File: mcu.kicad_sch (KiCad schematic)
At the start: 27 parts, among them J1 RP_DEBUG, SW1 BOOTSEL, SW2 RESET, U1 W25Q16JVSNIQ, U2 RP2040, Y1 12MHz

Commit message: WIP: display
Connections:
- net CAN_~{CS}: now also U2.7 (GPIO5); no longer U2.3 (GPIO1)
- net CAN_~{INT}: now also U2.3 (GPIO1); no longer U2.7 (GPIO5)
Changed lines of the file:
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@@
     (effects (font (size 1 1)) (justify left))
   )
-  (hierarchical_label "CAN_~{INT}" (shape input) (at 215.9 81.28 0)
+  (hierarchical_label "CAN_~{INT}" (shape input) (at 215.9 71.12 0)
     (effects (font (size 1 1)) (justify left))
   )
-  (hierarchical_label "CAN_~{CS}" (shape output) (at 215.9 71.12 0)
+  (hierarchical_label "CAN_~{CS}" (shape output) (at 215.9 81.28 0)
     (effects (font (size 1 1)) (justify left))
   )

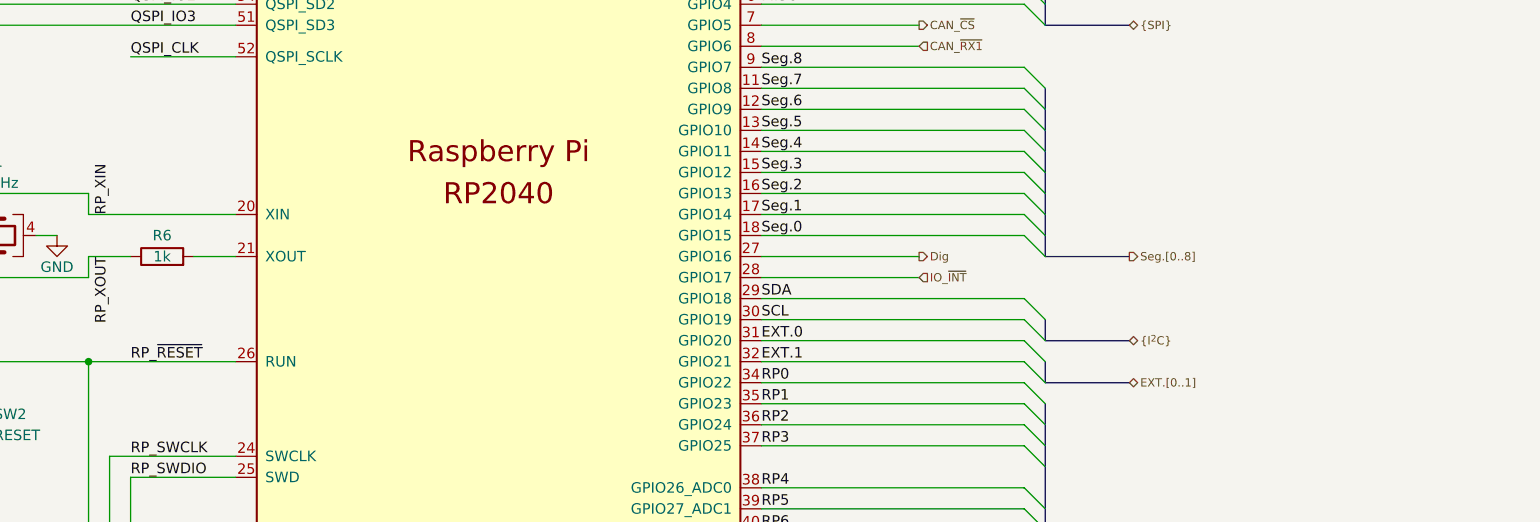
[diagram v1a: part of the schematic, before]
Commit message: rev1.1: Add I2C pullups
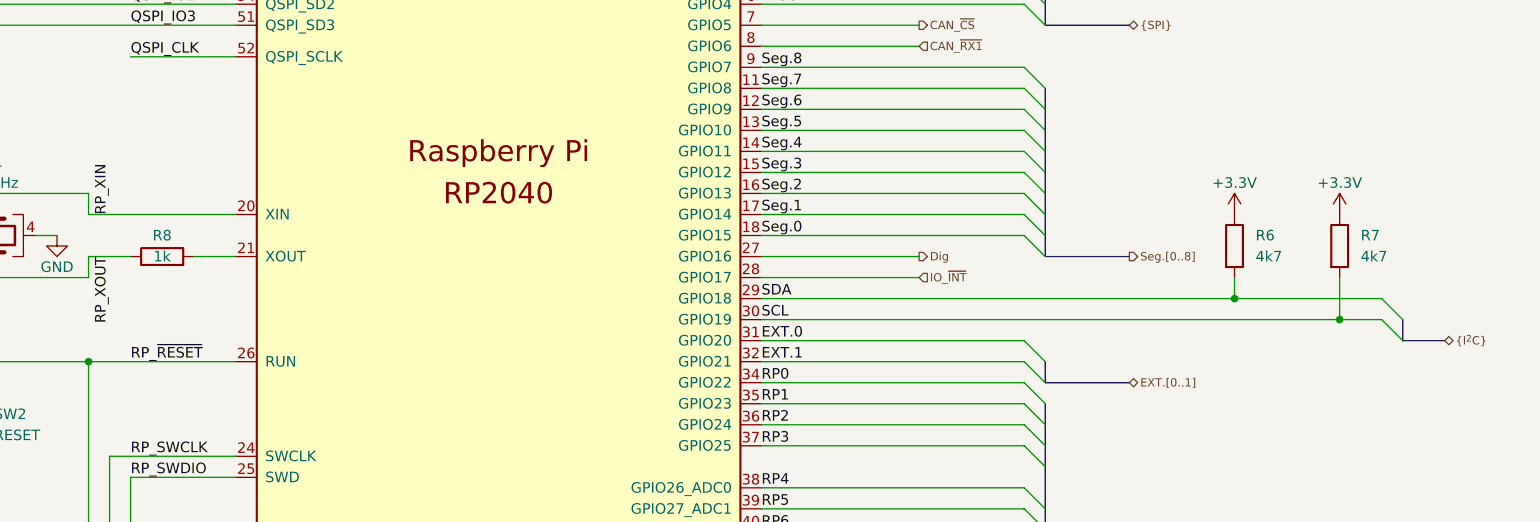
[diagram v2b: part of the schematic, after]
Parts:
- added R6, R7: 4k7, Resistor_SMD:R_0603_1608Metric, symbol Device:R
- renumbered R6 to R8
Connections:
- net +3V3: now also R6.1, R7.1
- net SCL: now also R7.2
- net SDA: now also R6.2
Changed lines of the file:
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@@
   (title_block
     (title "[canbrd] CAN/RS485 IO board")
-    (date "2022-02-24")
-    (rev "1.0")
+    (date "2022-03-18")
+    (rev "1.1")
   )
   (junction (at 173.99 48.26) (diameter 0) (color 0 0 0 0)
@@
   (junction (at 166.37 48.26) (diameter 0) (color 0 0 0 0)
   )
+  (junction (at 254 114.3) (diameter 0) (color 0 0 0 0)
+  )
   (junction (at 177.8 25.4) (diameter 0) (color 0 0 0 0)
   )
@@
   )
   (junction (at 127 38.1) (diameter 0) (color 0 0 0 0)
+  )
+  (junction (at 266.7 116.84) (diameter 0) (color 0 0 0 0)
   )
   (junction (at 85.09 111.76) (diameter 0) (color 0 0 0 0)
@@
     (stroke (width 0) (type default) (color 0 0 0 0))
   )
-  (bus_entry (at 231.14 116.84) (size -2.54 -2.54)
+  (bus_entry (at 274.32 116.84) (size -2.54 -2.54)
     (stroke (width 0) (type default) (color 0 0 0 0))
   )
@@
     (stroke (width 0) (type default) (color 0 0 0 0))
   )
-  (bus_entry (at 231.14 119.38) (size -2.54 -2.54)
+  (bus_entry (at 274.32 119.38) (size -2.54 -2.54)
     (stroke (width 0) (type default) (color 0 0 0 0))
   )
@@
     (stroke (width 0) (type default) (color 0 0 0 0))
   )
-  (wire (pts (xy 196.85 116.84) (xy 228.6 116.84))
+  (wire (pts (xy 196.85 116.84) (xy 266.7 116.84))
     (stroke (width 0) (type default) (color 0 0 0 0))
   )
@@
     (stroke (width 0) (type default) (color 0 0 0 0))
   )
+  (wire (pts (xy 266.7 111.76) (xy 266.7 116.84))
+    (stroke (width 0) (type default) (color 0 0 0 0))
+  )
   (wire (pts (xy 152.4 25.4) (xy 165.1 25.4))
     (stroke (width 0) (type default) (color 0 0 0 0))
@@
     (stroke (width 0) (type default) (color 0 0 0 0))
   )
+  (wire (pts (xy 254 114.3) (xy 271.78 114.3))
+    (stroke (width 0) (type default) (color 0 0 0 0))
+  )
   (wire (pts (xy 115.57 109.22) (xy 120.65 109.22))
     (stroke (width 0) (type default) (color 0 0 0 0))
@@
     (stroke (width 0) (type default) (color 0 0 0 0))
   )
-  (bus (pts (xy 241.3 119.38) (xy 231.14 119.38))
+  (bus (pts (xy 279.4 119.38) (xy 274.32 119.38))
     (stroke (width 0) (type default) (color 0 0 0 0))
   )
@@
     (stroke (width 0) (type default) (color 0 0 0 0))
   )
+  (wire (pts (xy 266.7 116.84) (xy 271.78 116.84))
+    (stroke (width 0) (type default) (color 0 0 0 0))
+  )
   (wire (pts (xy 177.8 35.56) (xy 177.8 38.1))
     (stroke (width 0) (type default) (color 0 0 0 0))
@@
     (stroke (width 0) (type default) (color 0 0 0 0))
   )
+  (wire (pts (xy 254 111.76) (xy 254 114.3))
+    (stroke (width 0) (type default) (color 0 0 0 0))
+  )
   (wire (pts (xy 196.85 81.28) (xy 215.9 81.28))
     (stroke (width 0) (type default) (color 0 0 0 0))
   )
-  (wire (pts (xy 196.85 114.3) (xy 228.6 114.3))
+  (wire (pts (xy 196.85 114.3) (xy 254 114.3))
     (stroke (width 0) (type default) (color 0 0 0 0))
   )
@@
     (stroke (width 0) (type default) (color 0 0 0 0))
   )
-  (bus (pts (xy 231.14 116.84) (xy 231.14 119.38))
+  (bus (pts (xy 274.32 116.84) (xy 274.32 119.38))
     (stroke (width 0) (type default) (color 0 0 0 0))
   )
@@
     (effects (font (size 1 1)) (justify left))
   )
-  (hierarchical_label "{I^{2}C}" (shape bidirectional) (at 241.3 119.38 0)
+  (hierarchical_label "{I^{2}C}" (shape bidirectional) (at 279.4 119.38 0)
     (effects (font (size 1 1)) (justify left))
   )
   (symbol (lib_id "power:GND") (at 76.2 167.64 0) (unit 1)
     (in_bom yes) (on_board yes)
-    (property "Reference" "#PWR027" (id 0) (at 76.2 173.99 0)
+    (property "Reference" "#PWR029" (id 0) (at 76.2 173.99 0)
       (effects (font (size 1.27 1.27)) hide)
     )
@@
   (symbol (lib_id "Device:R") (at 124.46 109.22 90) (unit 1)
     (in_bom yes) (on_board yes)
-    (property "Reference" "R6" (id 0) (at 124.46 106.68 90))
+    (property "Reference" "R8" (id 0) (at 124.46 106.68 90))
     (property "Value" "1k" (id 1) (at 124.46 109.22 90))
     (property "Footprint" "Resistor_SMD:R_0603_1608Metric" (id 2) (at 124.46 110.998 90)
@@
     (pin "2")
   )
+  (symbol (lib_id "power:+3.3V") (at 254 104.14 0) (unit 1)
+    (in_bom yes) (on_board yes)
+    (property "Reference" "#PWR021" (id 0) (at 254 107.95 0)
+      (effects (font (size 1.27 1.27)) hide)
+    )
+    (property "Value" "+3.3V" (id 1) (at 254 100.33 0))
+    (property "Footprint" "" (id 2) (at 254 104.14 0)
+      (effects (font (size 1.27 1.27)) hide)
+    )
+    (property "Datasheet" "" (id 3) (at 254 104.14 0)
+      (effects (font (size 1.27 1.27)) hide)
+    )
+    (pin "1")
+  )
   (symbol (lib_id "Device:C") (at 165.1 31.75 0) (unit 1)
     (in_bom yes) (on_board yes)
@@
   (symbol (lib_id "power:GND") (at 101.6 134.62 0) (unit 1)
     (in_bom yes) (on_board yes)
-    (property "Reference" "#PWR023" (id 0) (at 101.6 140.97 0)
+    (property "Reference" "#PWR025" (id 0) (at 101.6 140.97 0)
       (effects (font (size 1.27 1.27)) hide)
     )
@@
   (symbol (lib_id "power:GND") (at 111.76 106.68 0) (unit 1)
     (in_bom yes) (on_board yes)
-    (property "Reference" "#PWR021" (id 0) (at 111.76 113.03 0)
+    (property "Reference" "#PWR023" (id 0) (at 111.76 113.03 0)
       (effects (font (size 1.27 1.27)) hide)
     )
@@
     (pin "8")
     (pin "9")
+  )
+  (symbol (lib_id "Device:R") (at 254 107.95 0) (unit 1)
+    (in_bom yes) (on_board yes) (fields_autoplaced)
+    (property "Reference" "R6" (id 0) (at 256.54 106.6799 0)
+      (effects (font (size 1.27 1.27)) (justify left))
+    )
+    (property "Value" "4k7" (id 1) (at 256.54 109.2199 0)
+      (effects (font (size 1.27 1.27)) (justify left))
+    )
+    (property "Footprint" "Resistor_SMD:R_0603_1608Metric" (id 2) (at 252.222 107.95 90)
+      (effects (font (size 1.27 1.27)) hide)
+    )
+    (property "Datasheet" "~" (id 3) (at 254 107.95 0)
+      (effects (font (size 1.27 1.27)) hide)
+    )
+    (pin "1")
+    (pin "2")
   )
   (symbol (lib_id "power:GND") (at 88.9 86.36 0) (unit 1)
@@
   (symbol (lib_id "power:+3.3V") (at 76.2 137.16 0) (unit 1)
     (in_bom yes) (on_board yes)
-    (property "Reference" "#PWR024" (id 0) (at 76.2 140.97 0)
+    (property "Reference" "#PWR026" (id 0) (at 76.2 140.97 0)
       (effects (font (size 1.27 1.27)) hide)
     )
@@
   (symbol (lib_id "power:GND") (at 152.4 152.4 0) (unit 1)
     (in_bom yes) (on_board yes)
-    (property "Reference" "#PWR025" (id 0) (at 152.4 158.75 0)
+    (property "Reference" "#PWR027" (id 0) (at 152.4 158.75 0)
       (effects (font (size 1.27 1.27)) hide)
     )
@@
     (pin "2")
   )
+  (symbol (lib_id "Device:R") (at 266.7 107.95 0) (unit 1)
+    (in_bom yes) (on_board yes) (fields_autoplaced)
+    (property "Reference" "R7" (id 0) (at 269.24 106.6799 0)
+      (effects (font (size 1.27 1.27)) (justify left))
+    )
+    (property "Value" "4k7" (id 1) (at 269.24 109.2199 0)
+      (effects (font (size 1.27 1.27)) (justify left))
+    )
+    (property "Footprint" "Resistor_SMD:R_0603_1608Metric" (id 2) (at 264.922 107.95 90)
+      (effects (font (size 1.27 1.27)) hide)
+    )
+    (property "Datasheet" "~" (id 3) (at 266.7 107.95 0)
+      (effects (font (size 1.27 1.27)) hide)
+    )
+    (pin "1")
+    (pin "2")
+  )
   (symbol (lib_id "Device:R") (at 57.15 82.55 0) (unit 1)
     (in_bom yes) (on_board yes)
@@
   (symbol (lib_id "power:GND") (at 85.09 114.3 0) (unit 1)
     (in_bom yes) (on_board yes)
-    (property "Reference" "#PWR022" (id 0) (at 85.09 120.65 0)
+    (property "Reference" "#PWR024" (id 0) (at 85.09 120.65 0)
       (effects (font (size 1.27 1.27)) hide)
     )
@@
   (symbol (lib_id "power:GND") (at 165.1 152.4 0) (unit 1)
     (in_bom yes) (on_board yes)
-    (property "Reference" "#PWR026" (id 0) (at 165.1 158.75 0)
+    (property "Reference" "#PWR028" (id 0) (at 165.1 158.75 0)
       (effects (font (size 1.27 1.27)) hide)
     )
@@
     (pin "2")
   )
+  (symbol (lib_id "power:+3.3V") (at 266.7 104.14 0) (unit 1)
+    (in_bom yes) (on_board yes)
+    (property "Reference" "#PWR022" (id 0) (at 266.7 107.95 0)
+      (effects (font (size 1.27 1.27)) hide)
+    )
+    (property "Value" "+3.3V" (id 1) (at 266.7 100.33 0))
+    (property "Footprint" "" (id 2) (at 266.7 104.14 0)
+      (effects (font (size 1.27 1.27)) hide)
+    )
+    (property "Datasheet" "" (id 3) (at 266.7 104.14 0)
+      (effects (font (size 1.27 1.27)) hide)
+    )
+    (pin "1")
+  )
 )

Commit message: lots changed
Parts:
- removed R6, R7: 4k7, Resistor_SMD:R_0603_1608Metric, symbol Device:R
- renumbered R8 to R6
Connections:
- net EXT.0 is gone; now on net RP2: U2.31 (GPIO20)
- net EXT.1 is gone; now on net RP3: U2.32 (GPIO21)
- net SCL is gone; now on net RP1: U2.30 (GPIO19)
- net SDA is gone; now on net RP0: U2.29 (GPIO18)
- net RP0: no longer U2.34 (GPIO22)
- net RP1: no longer U2.35 (GPIO23)
- net RP2: no longer U2.36 (GPIO24)
- net RP3: no longer U2.37 (GPIO25)
- net RP4: now also U2.34 (GPIO22); no longer U2.38 (GPIO26_ADC0)
- net RP5: now also U2.35 (GPIO23); no longer U2.39 (GPIO27_ADC1)
- net RP6: now also U2.36 (GPIO24); no longer U2.40 (GPIO28_ADC2)
- net RP7: now also U2.37 (GPIO25); no longer U2.41 (GPIO29_ADC3)
- net IO_~{INT} renamed IO_~{CS}
- new net RP10: U2.40 (GPIO28_ADC2)
- new net RP11: U2.41 (GPIO29_ADC3)
- new net RP8: U2.38 (GPIO26_ADC0)
- new net RP9: U2.39 (GPIO27_ADC1)

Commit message: things changed
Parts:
- added C14, C17: 100n, Capacitor_SMD:C_0603_1608Metric, symbol Device:C
- added R5, R6: 130, Resistor_SMD:R_0603_1608Metric, symbol Device:R
- added R8: DNP, Resistor_SMD:R_0603_1608Metric, symbol Device:R_Small
- renumbered C14 to C15, C15 to C16, R5 to R7, R6 to R9
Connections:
- net GND: now also C14.2, C17.2
- net MOSI: now also R6.2; no longer U2.5 (GPIO3)
- net RP_~{RESET}: now also C17.1
- net SCK: now also R5.2; no longer U2.4 (GPIO2)
- net ~{BOOTSEL}: now also C14.1
- net RP_SWCLK renamed SWCLK
- net RP_SWDIO renamed SWDIO
- net RP_XIN renamed XIN
- net XIN: now also R8.1
- net RP_XOUT renamed XOUT
- net XOUT: now also R8.2
- net USB_XDM renamed xUSB_DM
- net USB_XDP renamed xUSB_DP
- new net xMOSI: R6.1, U2.5 (GPIO3)
- new net xSCK: R5.1, U2.4 (GPIO2)
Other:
- moved on the sheet: C11, C12, J1, R1, SW2

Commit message: isolate and other stuff
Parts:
- added TP1, TP2, TP3: TestPoint, TestPoint:TestPoint_THTPad_D2.0mm_Drill1.0mm, symbol Connector:TestPoint
- C15, C16: value ??? -> 10p
- R5, R6: value 130 -> 100
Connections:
- net RP_~{RESET}: now also TP1.1
- net SWCLK: now also TP2.1
- net SWDIO: now also TP3.1
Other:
- title: [canbrd] CAN/RS485 IO board -> [canbrd] CAN IO board

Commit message: things changed
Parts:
- added R10, R11: 2.2k, Resistor_SMD:R_0603_1608Metric, symbol Device:R
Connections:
- net CAN_~{RX1} is gone; now on net Seg.8: U2.8 (GPIO6)
- net Seg.0: now also U2.17 (GPIO14); no longer U2.18 (GPIO15)
- net Seg.1: now also U2.16 (GPIO13); no longer U2.17 (GPIO14)
- net Seg.2: now also U2.15 (GPIO12); no longer U2.16 (GPIO13)
- net Seg.3: now also U2.14 (GPIO11); no longer U2.15 (GPIO12)
- net Seg.4: now also U2.13 (GPIO10); no longer U2.14 (GPIO11)
- net Seg.5: now also U2.12 (GPIO9); no longer U2.13 (GPIO10)
- net Seg.6: now also U2.11 (GPIO8); no longer U2.12 (GPIO9)
- net Seg.7: now also U2.9 (GPIO7); no longer U2.11 (GPIO8)
- net Seg.8: no longer U2.9 (GPIO7)
- net +3V3 renamed +3.3V
- net +3.3V: now also R10.1, R11.1
- net Dig renamed Dig1
- net RP10 renamed I_meas
- net RP11 renamed U_meas
- net RP8 renamed SDA
- net SDA: now also R10.2
- net RP9 renamed SCL
- net SCL: now also R11.2
- new net Dig0: U2.18 (GPIO15)
